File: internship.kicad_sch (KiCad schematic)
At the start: 83 parts, among them J1 3.7V_LIPO, J2 USB_C_16P, J3 RC_RECEIVER, J4 M1_MOTOR, J5 M2_MOTOR, J6 M3_MOTOR, J7 M4_MOTOR, J8 GPS_MODULE, J9 I2C_COMPASS, Q1 AO3400A, Q2 AO3400A, Q3 AO3400A, Q4 AO3400A, Q5 AO3400A, Q6 AO3400A, SW1 RESET, SW2 BOOT, SW3 PWR_SW, U1 ESP32-S3-WROOM-1, U2 ICM-42688-P, U4 TP4056, U5 AP2112K-3.3, U6 BMP280

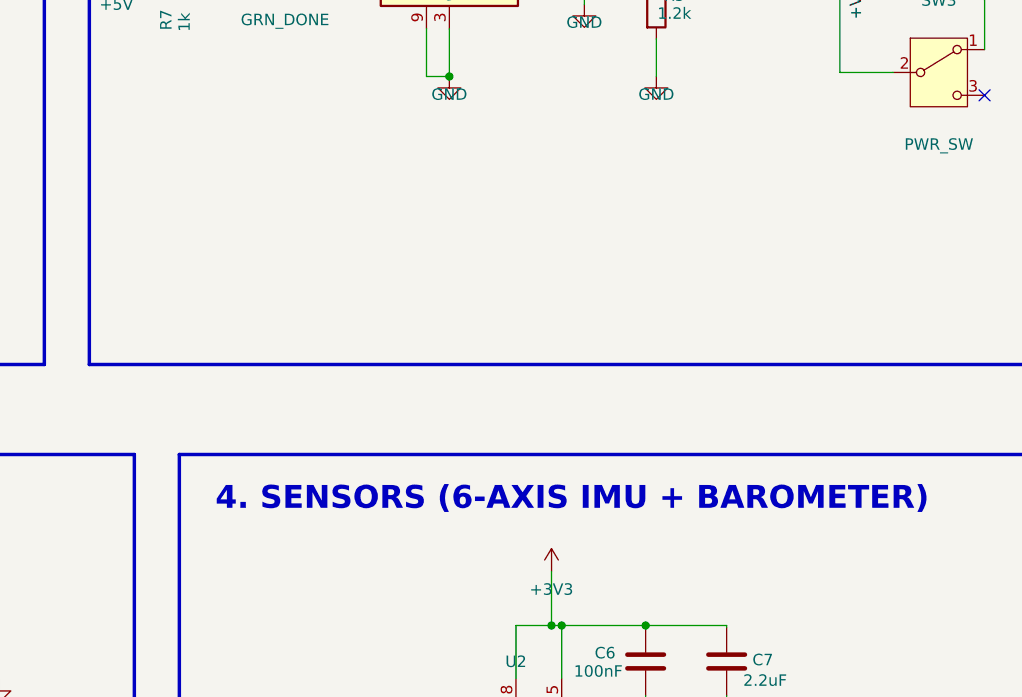
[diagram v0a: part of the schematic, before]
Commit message: Add secondary MPU-6050 IMU (U3 + C4, C5, C8) on B.Cu and update Gerbers/Manufacturing Pack
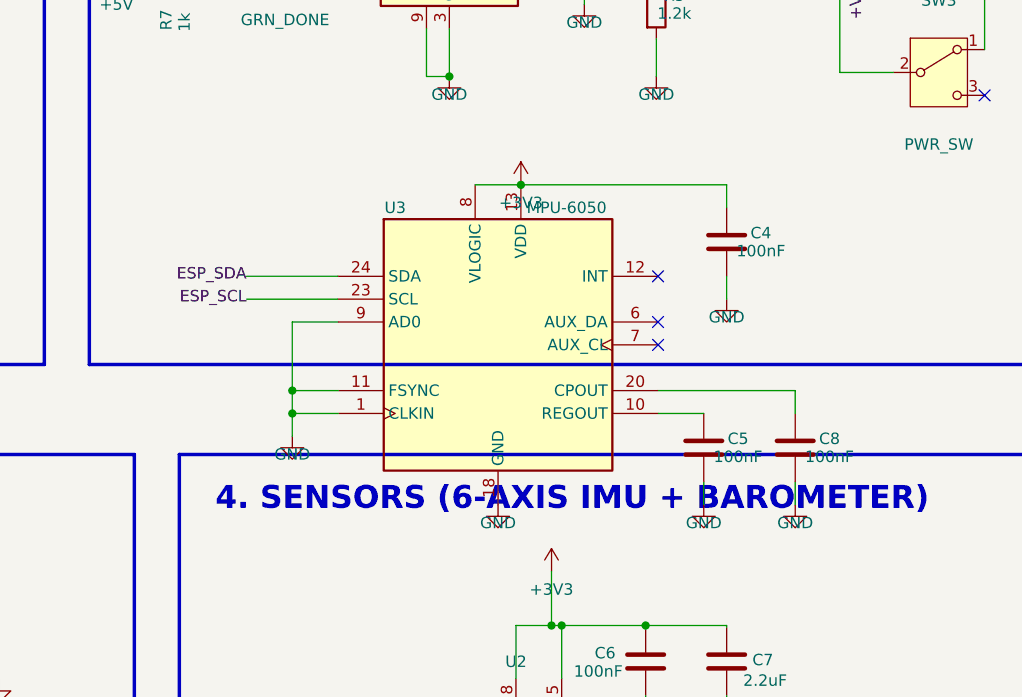
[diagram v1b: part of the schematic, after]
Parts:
- added C4, C5, C8: 100nF, Capacitor_SMD:C_0603_1608Metric, symbol Device:C
- added U3: MPU-6050, Sensor_Motion:InvenSense_QFN-24_4x4mm_P0.5mm, symbol Sensor_Motion:MPU-6050
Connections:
- net +3V3: now also C4.1, U3.13 (VDD), U3.8 (VLOGIC)
- net ESP_SCL: now also U3.23 (SCL)
- net ESP_SDA: now also U3.24 (SDA)
- net GND: now also C4.2, C5.2, C8.2, U3.1 (CLKIN), U3.11 (FSYNC), U3.18 (GND), U3.9 (AD0)
- new net: C8.1, U3.20 (CPOUT)
- new net: C5.1, U3.10 (REGOUT)
- no-connect marks 18 -> 21
